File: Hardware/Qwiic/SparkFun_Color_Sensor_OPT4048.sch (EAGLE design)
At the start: 25 parts, among them J1 QWIIC_RIGHT_ANGLE, J2 QWIIC_RIGHT_ANGLE, U1 OPT4048

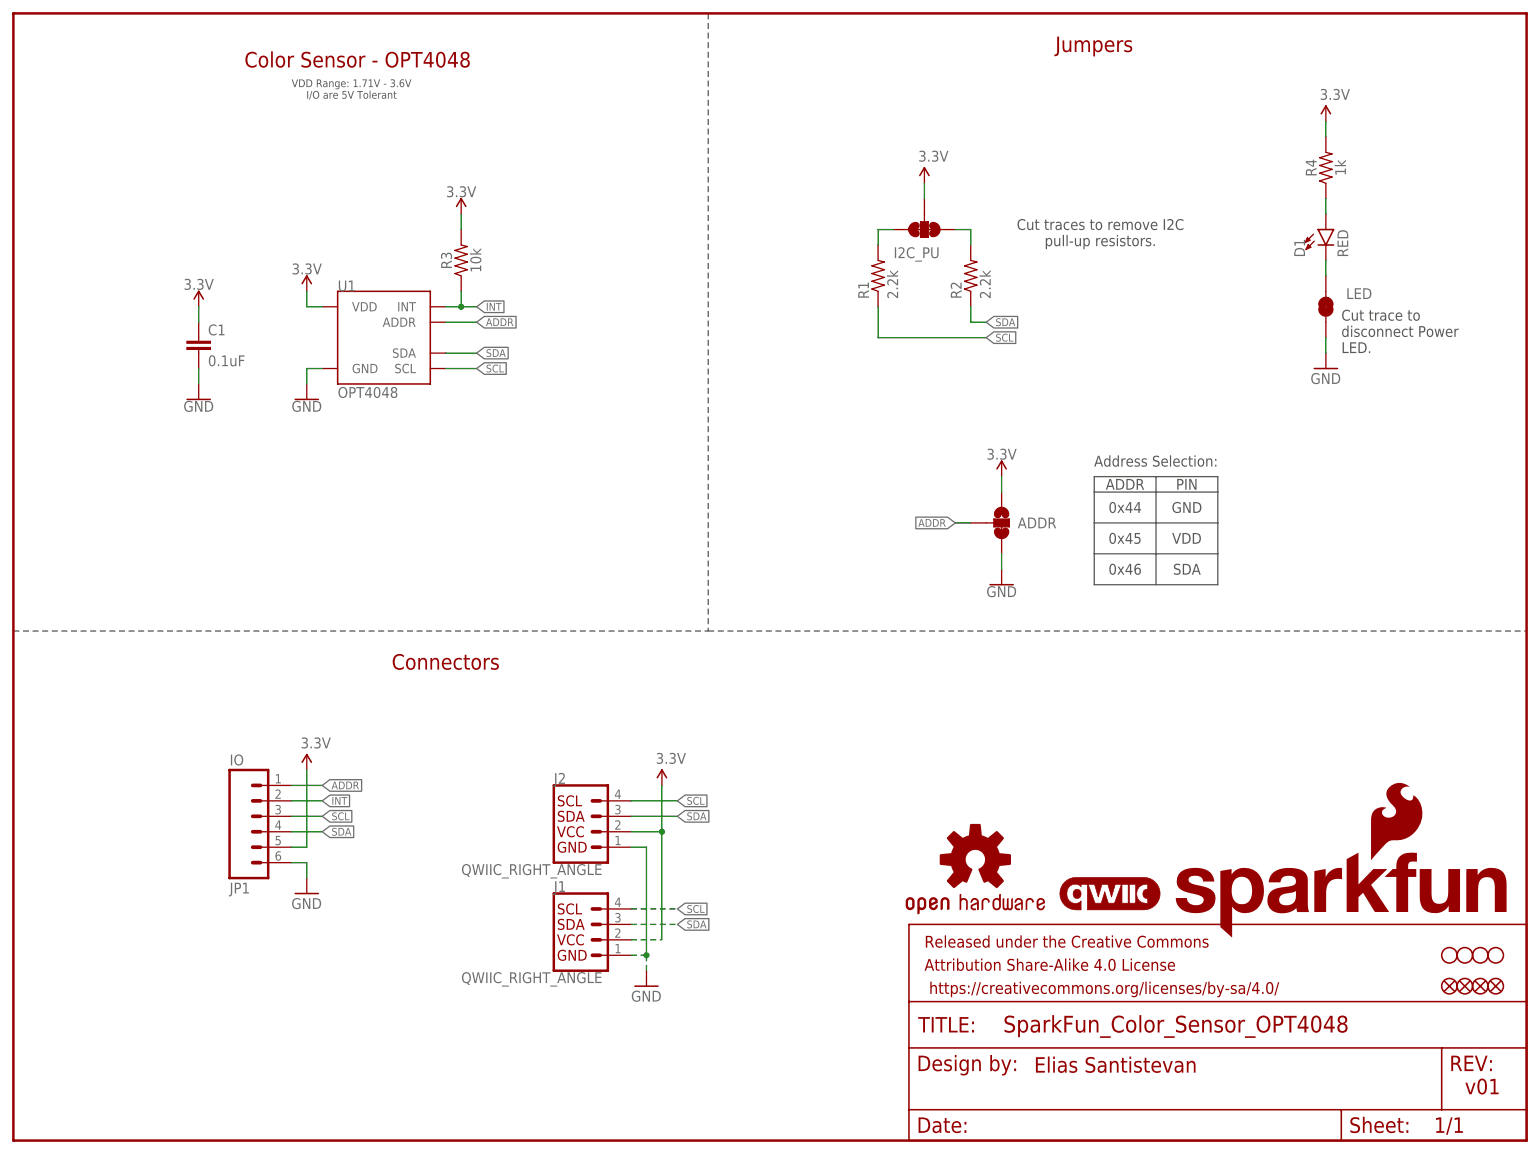
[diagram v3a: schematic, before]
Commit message: Routes Qwiic board
* Adds ADDR2 jumper for SDA
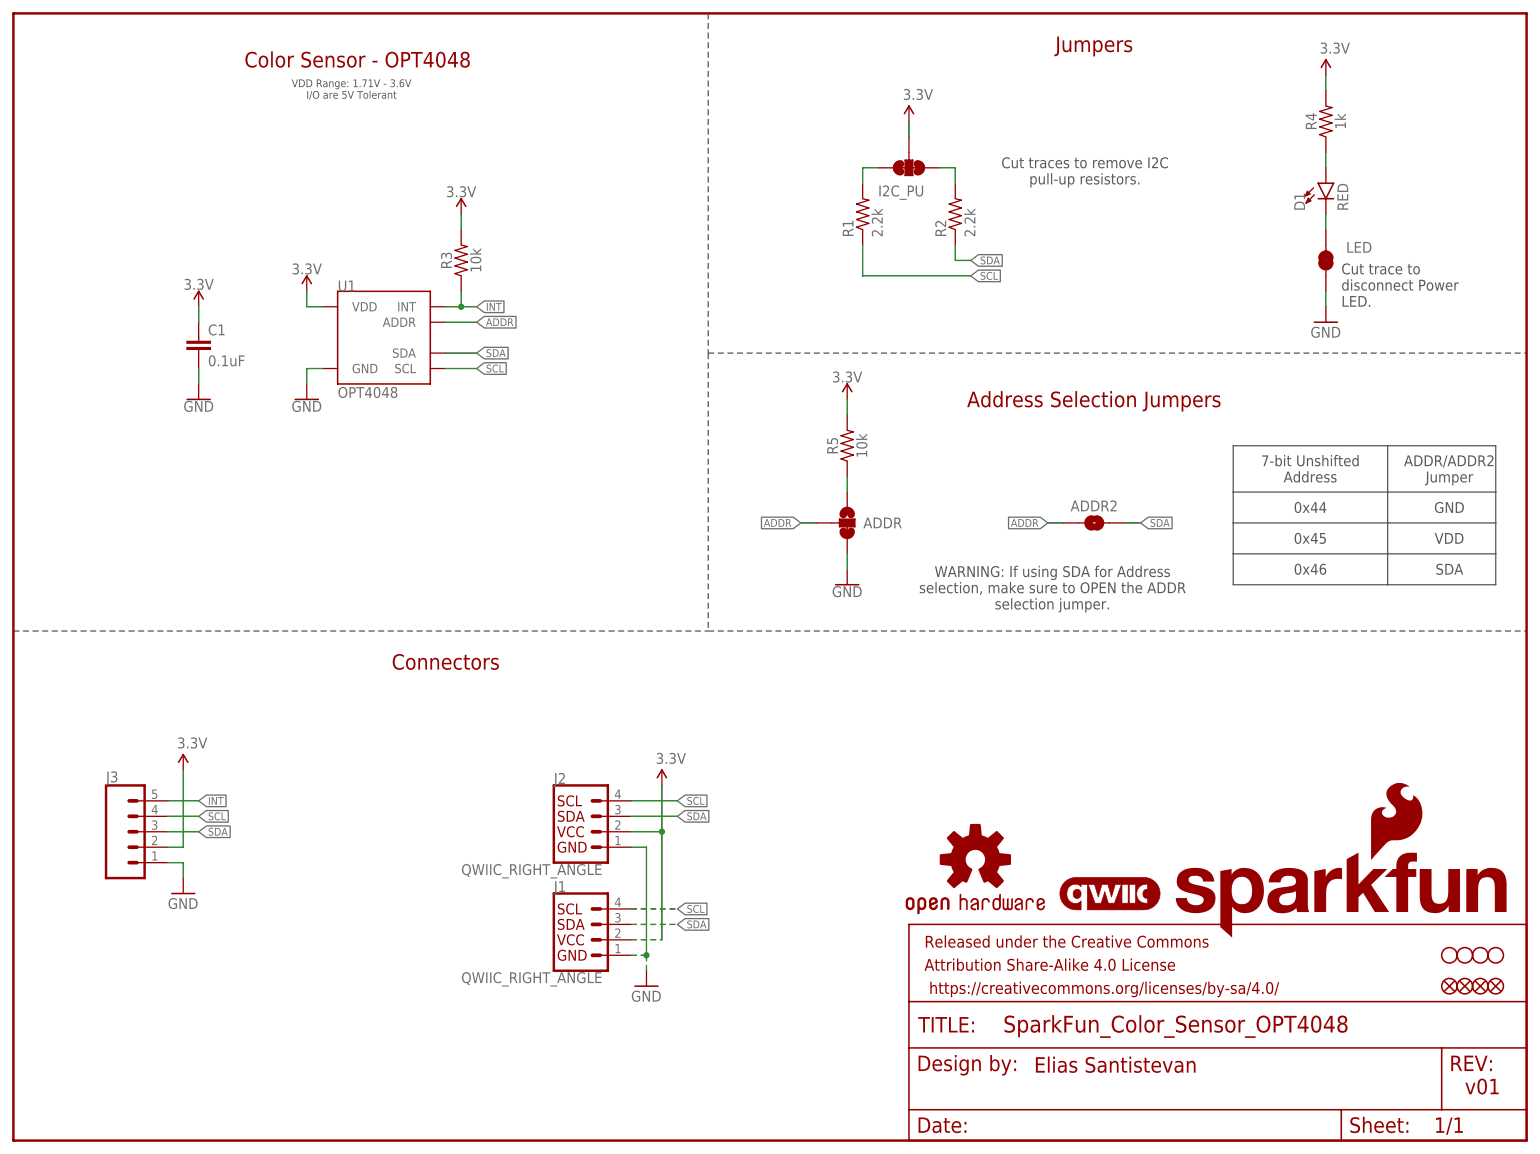
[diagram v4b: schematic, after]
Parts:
- removed JP1: IO, SparkFun-Connectors:CONN_06NO_SILK_NO_POP
- added ADDR2: JUMPER-SMT_2_NO_SILK, SparkFun-Jumpers:JUMPER-SMT_2_NO_SILK
- added J3: (no value), SparkFun-Connectors:CONN_05NO_SILK
- added R5: 10k, SparkFun-Resistors:10KOHM-0603-1/10W-1%
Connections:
- new net N$1: ADDR.1, R5.1
- net 3.3V: now also J3.2, R5.2; no longer ADDR.1, JP1.5
- net ADDR: now also ADDR2.1; no longer JP1.1
- net GND: now also J3.1; no longer JP1.6
- net INT: now also J3.5; no longer JP1.2
- net SCL: now also J3.4; no longer JP1.3
- net SDA: now also ADDR2.2, J3.3; no longer JP1.4
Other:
- note added: "7-bit Unshifted Address"
- note added: "ADDR/ADDR2 Jumper"
- note added: "Address Selection Jumpers"
- note added: "WARNING: If using SDA for Address selection, make sure to OPEN the ADDR selection jumper."
- note removed: "ADDR"
- note removed: "Address Selection:"
- note removed: "PIN"
- moved on the sheet: ADDR, D1, I2C_PU, LED, R1, R2, R4

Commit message: Improves ground pour
* Improves schematic aesthetic
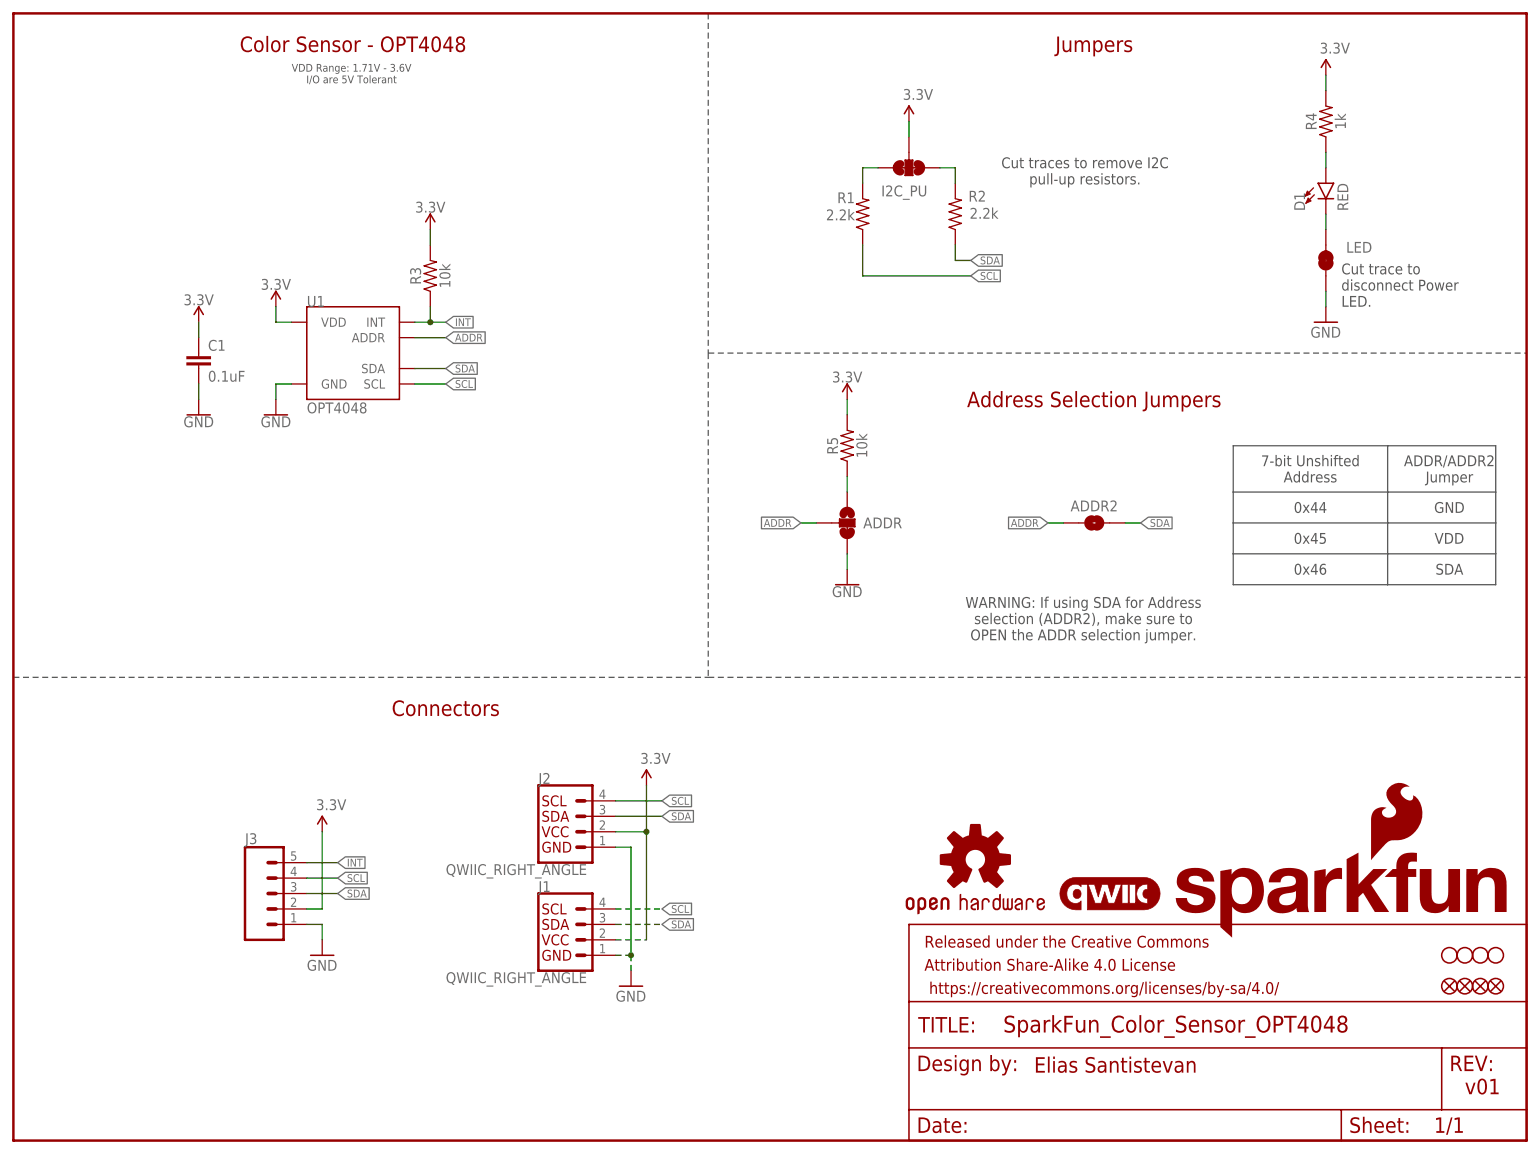
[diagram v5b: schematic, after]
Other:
- note added: "WARNING: If using SDA for Address selection (ADDR2), make sure to OPEN the ADDR selection jumper."
- note removed: "WARNING: If using SDA for Address selection, make sure to OPEN the ADDR selection jumper."
- moved on the sheet: C1, J1, J2, J3, R3, U1

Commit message: Finishes routing Qwiic mini
* Adds silk to Qwiic mini
* Adds ordering instructions
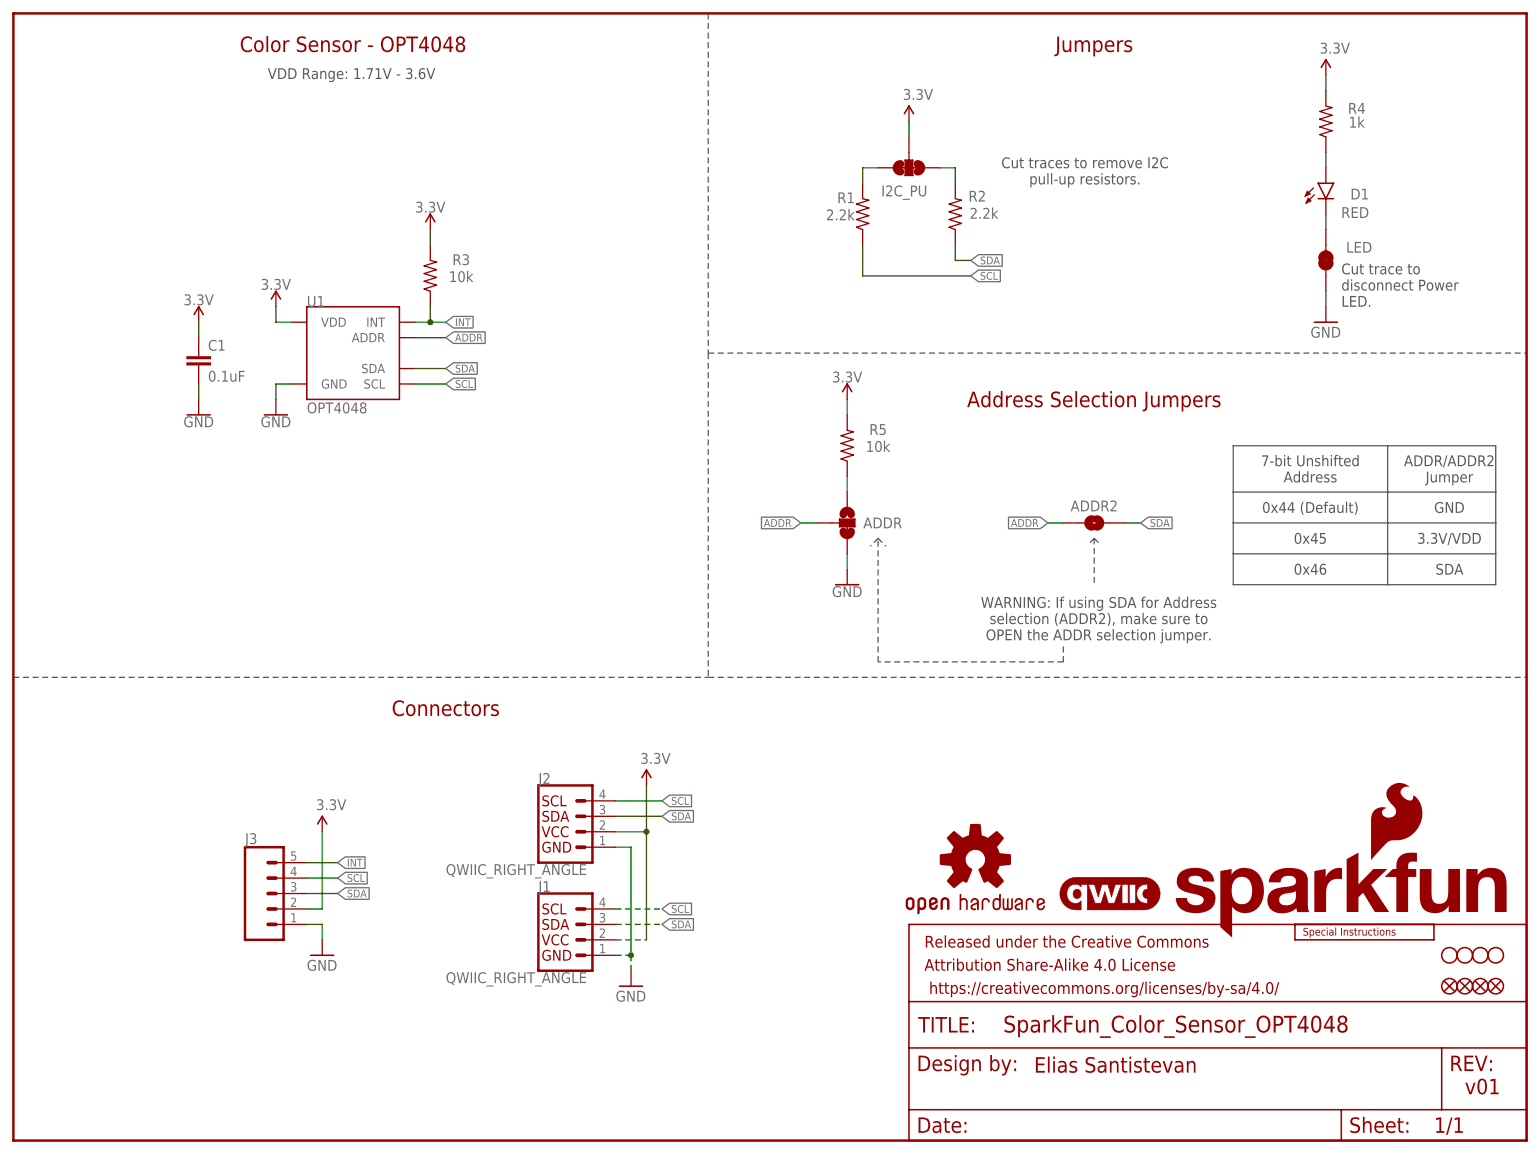
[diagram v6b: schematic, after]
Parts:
- added LOGO4: SPECIAL_INSTRUCTIONS-ORDERING, SparkFun-Aesthetics:SPECIAL_INSTRUCTIONS-ORDERING
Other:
- note added: "0x44 (Default)"
- note added: "3.3V/VDD"
- note added: "VDD Range: 1.71V - 3.6V"
- note removed: "0x44"
- note removed: "VDD"
- note removed: "VDD Range: 1.71V - 3.6V I/O are 5V Tolerant"
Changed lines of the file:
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@@
 <part name="GND5" library="SparkFun-PowerSymbols" deviceset="GND" device=""/>
 <part name="R5" library="SparkFun-Resistors" deviceset="10KOHM" device="-0603-1/10W-1%" value="10k"/>
+<part name="LOGO4" library="SparkFun-Aesthetics" deviceset="SPECIAL_INSTRUCTIONS" device="-ORDERING"/>
 </parts>
 <sheets>
@@
 <wire x1="114.3" y1="76.2" x2="248.92" y2="76.2" width="0.2032" layer="97" style="longdash"/>
 <wire x1="114.3" y1="185.42" x2="114.3" y2="129.54" width="0.2032" layer="97" style="longdash"/>
-<text x="55.626" y="175.514" size="1.27" layer="97" font="vector" align="center">VDD Range: 1.71V - 3.6V
-I/O are 5V Tolerant</text>
+<text x="55.626" y="175.514" size="1.778" layer="97" font="vector" align="center">VDD Range: 1.71V - 3.6V</text>
 <text x="238.76" y="7.62" size="2.54" layer="94" font="vector">v01</text>
 <text x="177.8" y="180.34" size="2.54" layer="94" font="vector" align="center">Jumpers</text>
@@
 <wire x1="243.84" y1="101.6" x2="243.84" y2="106.68" width="0.127" layer="97"/>
 <wire x1="243.84" y1="106.68" x2="200.66" y2="106.68" width="0.127" layer="97"/>
-<text x="213.36" y="104.14" size="1.778" layer="97" font="vector" align="center">0x44</text>
+<text x="213.36" y="104.14" size="1.778" layer="97" font="vector" align="center">0x44 (Default)</text>
 <text x="213.36" y="99.06" size="1.778" layer="97" font="vector" align="center">0x45</text>
 <text x="213.36" y="93.98" size="1.778" layer="97" font="vector" align="center">0x46</text>
@@
 <wire x1="200.66" y1="91.44" x2="226.06" y2="91.44" width="0.127" layer="97"/>
 <text x="236.22" y="104.14" size="1.778" layer="97" font="vector" align="center">GND</text>
-<text x="236.22" y="99.06" size="1.778" layer="97" font="vector" align="center">VDD</text>
+<text x="236.22" y="99.06" size="1.778" layer="97" font="vector" align="center">3.3V/VDD</text>
 <text x="236.22" y="93.98" size="1.778" layer="97" font="vector" align="center">SDA</text>
 <wire x1="226.06" y1="91.44" x2="243.84" y2="91.44" width="0.127" layer="97"/>
@@
 <text x="236.22" y="110.49" size="1.778" layer="97" font="vector" align="center">ADDR/ADDR2
 Jumper</text>
-<text x="176.022" y="85.852" size="1.778" layer="97" font="vector" align="center">WARNING: If using SDA for Address
+<text x="178.562" y="85.852" size="1.778" layer="97" font="vector" align="center">WARNING: If using SDA for Address
 selection (ADDR2), make sure to
 OPEN the ADDR selection jumper.</text>
@@
 <wire x1="114.3" y1="129.54" x2="248.92" y2="129.54" width="0.1524" layer="97" style="longdash"/>
 <text x="177.8" y="121.92" size="2.54" layer="94" font="vector" align="center">Address Selection Jumpers</text>
+<wire x1="177.8" y1="99.06" x2="177.8" y2="91.44" width="0.1524" layer="97" style="dashdot"/>
+<wire x1="177.8" y1="99.06" x2="176.784" y2="98.044" width="0.1524" layer="97" style="dashdot"/>
+<wire x1="177.8" y1="99.06" x2="178.816" y2="98.044" width="0.1524" layer="97" style="dashdot"/>
+<wire x1="172.72" y1="81.28" x2="172.72" y2="78.74" width="0.1524" layer="97" style="dashdot"/>
+<wire x1="172.72" y1="78.74" x2="142.24" y2="78.74" width="0.1524" layer="97" style="dashdot"/>
+<wire x1="142.24" y1="78.74" x2="142.24" y2="99.06" width="0.1524" layer="97" style="dashdot"/>
+<wire x1="142.24" y1="99.06" x2="140.97" y2="97.79" width="0.1524" layer="97" style="dashdot"/>
+<wire x1="142.24" y1="99.06" x2="143.51" y2="97.79" width="0.1524" layer="97" style="dashdot"/>
 </plain>
 <instances>
@@
 </instance>
 <instance part="D1" gate="G$1" x="215.9" y="157.48" smashed="yes">
-<attribute name="NAME" x="212.471" y="152.908" size="1.778" layer="95" font="vector" rot="R90"/>
-<attribute name="VALUE" x="217.805" y="152.908" size="1.778" layer="96" font="vector" rot="R90" align="top-left"/>
+<attribute name="NAME" x="223.012" y="156.591" size="1.778" layer="95" font="vector" rot="R180"/>
+<attribute name="VALUE" x="223.012" y="151.765" size="1.778" layer="96" font="vector" rot="R180" align="top-left"/>
 </instance>
 <instance part="R4" gate="G$1" x="215.9" y="167.64" smashed="yes" rot="R90">
-<attribute name="NAME" x="214.376" y="167.64" size="1.778" layer="95" font="vector" rot="R90" align="bottom-center"/>
-<attribute name="VALUE" x="217.424" y="167.64" size="1.778" layer="96" font="vector" rot="R90" align="top-center"/>
+<attribute name="NAME" x="220.98" y="170.688" size="1.778" layer="95" font="vector" rot="R180" align="bottom-center"/>
+<attribute name="VALUE" x="220.98" y="166.624" size="1.778" layer="96" font="vector" rot="R180" align="top-center"/>
 </instance>
 <instance part="LED" gate="G$1" x="215.9" y="144.78" smashed="yes" rot="R90">
@@
 </instance>
 <instance part="R3" gate="G$1" x="68.58" y="142.24" smashed="yes" rot="R90">
-<attribute name="NAME" x="67.056" y="142.24" size="1.778" layer="95" font="vector" rot="R90" align="bottom-center"/>
-<attribute name="VALUE" x="70.104" y="142.24" size="1.778" layer="96" font="vector" rot="R90" align="top-center"/>
+<attribute name="NAME" x="73.66" y="145.796" size="1.778" layer="95" font="vector" rot="R180" align="bottom-center"/>
+<attribute name="VALUE" x="73.66" y="141.224" size="1.778" layer="96" font="vector" rot="R180" align="top-center"/>
 </instance>
 <instance part="SUPPLY7" gate="G$1" x="68.58" y="149.86" smashed="yes">
@@
 </instance>
 <instance part="R5" gate="G$1" x="137.16" y="114.3" smashed="yes" rot="R90">
-<attribute name="NAME" x="135.636" y="114.3" size="1.778" layer="95" font="vector" rot="R90" align="bottom-center"/>
-<attribute name="VALUE" x="138.684" y="114.3" size="1.778" layer="96" font="vector" rot="R90" align="top-center"/>
+<attribute name="NAME" x="142.24" y="117.856" size="1.778" layer="95" font="vector" rot="R180" align="bottom-center"/>
+<attribute name="VALUE" x="142.24" y="113.284" size="1.778" layer="96" font="vector" rot="R180" align="top-center"/>
 </instance>
+<instance part="LOGO4" gate="G$1" x="210.82" y="33.02" smashed="yes"/>
 </instances>
 <busses>
